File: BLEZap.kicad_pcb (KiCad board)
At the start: 2 copper layers, 38.1 x 22.9 mm, 12 parts, among them P1 PRG_HEADER, P2 INPUT_HEADER, P3 CONN_01X02, Q1 IRLML6344, U1 Core51822B

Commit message: PCB Ready
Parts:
- removed JP1, JP2: Jumper, Resistors_SMD:R_1206
- added REF**: MountingHole_2.7mm_M2.5, Mounting_Holes:MountingHole_2.7mm_M2.5, F.Cu at (89.7, 88.1)
- P1: footprint KevinLibrary:POGO_PIN_PAD_1X4 -> Pin_Headers:Pin_Header_Straight_1x04
- P2: footprint KevinLibrary:Pin_Header_Straight_1x04_HB -> Pin_Headers:Pin_Header_Straight_1x04
- moved P1 7.62 mm to (79.5, 78.7), turned to 90 degrees
- moved R4 7.03 mm to (87.4, 82.8)
- moved U1 2.30 mm to (103.9, 88.1), turned to 0 degrees
- moved P2 1.70 mm to (79.5, 96.8)
- moved Q1 1.61 mm to (85.1, 91.4)
- moved R2 1.52 mm to (78.7, 82.8)
- moved R1 1.31 mm to (81.5, 82.8)
- moved R3 1.13 mm to (84.3, 82.8)
- moved D1 1.05 mm to (81.5, 88.9)
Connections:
- P3 pad 1: Net-(JP2-Pad2) -> Net-(D1-Pad1)
- R2 pad 2: Net-(JP2-Pad2) -> Net-(D1-Pad1)
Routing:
- net Net-(JP2-Pad2): track 16.5 -> 0.00 mm
- net /RELAY: track 32.0 -> 16.9 mm, vias 0 -> 1
- net GNDD: track 24.5 -> 9.65 mm
- net /CFG_BTN: track 27.1 -> 17.9 mm, vias 0 -> 1
- net Net-(Q1-Pad1): track 0.00 -> 7.79 mm, vias 0 -> 2
- net Net-(R4-Pad2): track 13.6 -> 7.33 mm
- net /SWDIO: track 30.0 -> 26.7 mm, vias 0 -> 1
- net GND: track 13.2 -> 10.3 mm
- net /SWCLK: track 32.6 -> 29.9 mm, vias 0 -> 1
- net Net-(D1-Pad1): track 32.6 -> 30.3 mm
- net VDD: track 43.9 -> 42.5 mm
- added copper zone on B.Cu, net GNDD
- added copper zone on F.Cu, net GNDD
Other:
- net class Default: clearance 0.3048 -> 0.254; trace_width 0.3048 -> 0.1524; via_dia 2.54 -> 0.6858; via_drill 0.8382 -> 0.3302
- net class Power added: clearance 0.3048, trace_width 0.3048, via_dia 0.6858, via_drill 0.3302
- rule trace_clearance: 0.3048 -> 0.254
- rule trace_min: 0.3048 -> 0.1524
- rule via_min_drill: 0.8382 -> 0.3302
- rule via_min_size: 2.54 -> 0.6858

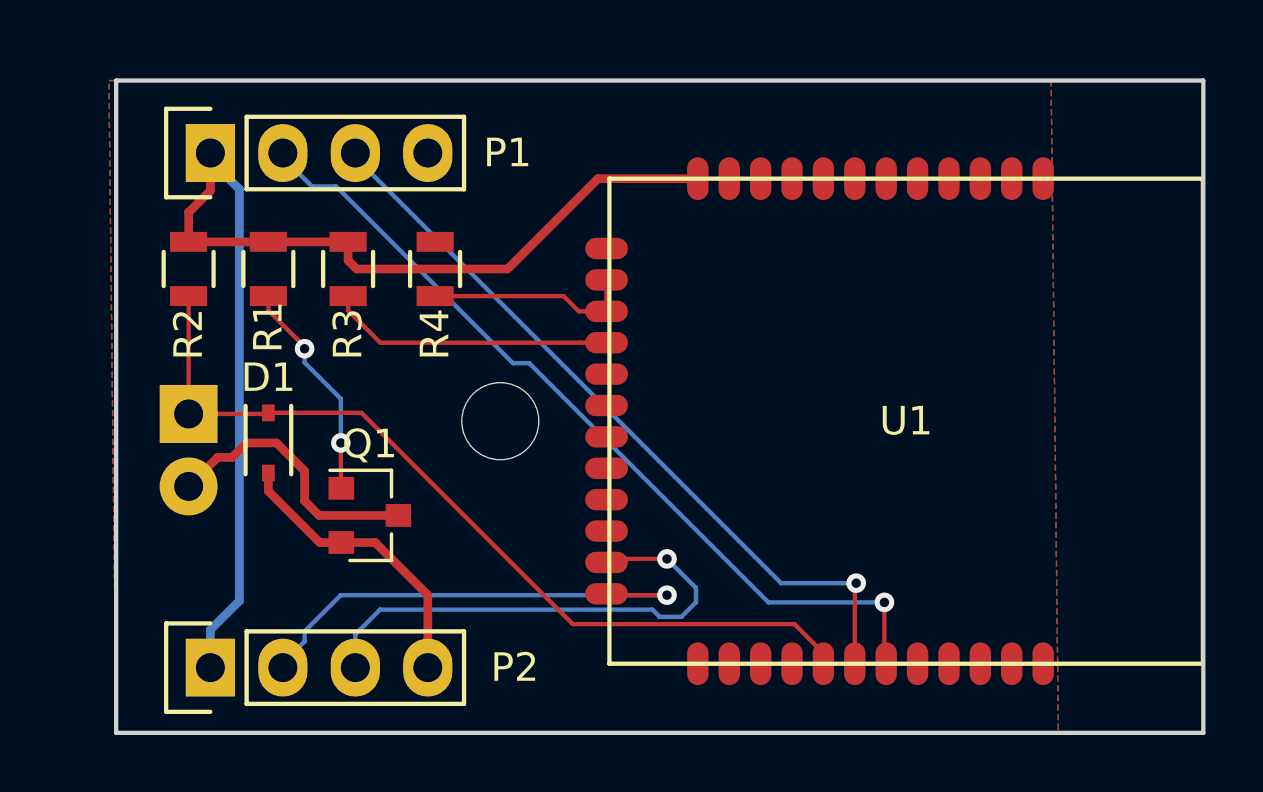
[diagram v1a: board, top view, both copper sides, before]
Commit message: SWD Swap
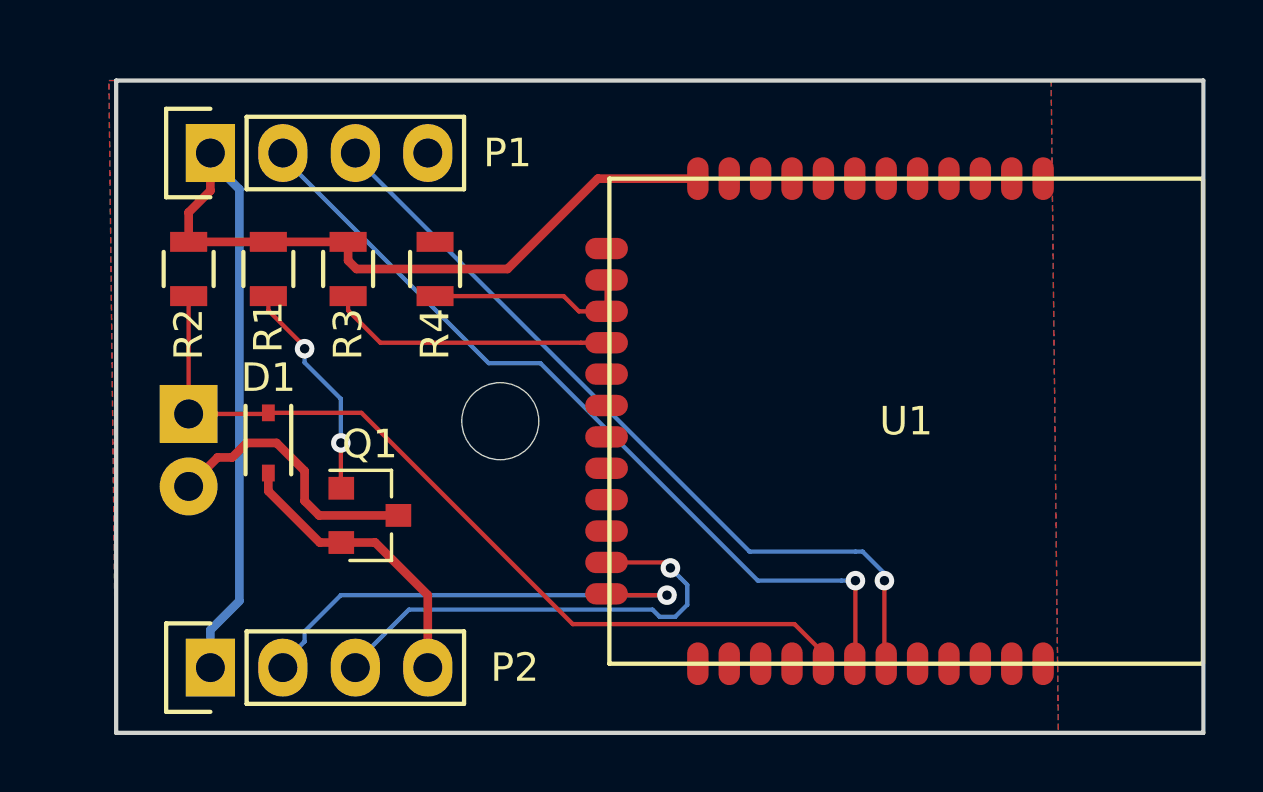
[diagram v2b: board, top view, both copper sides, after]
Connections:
- P1 pad 2: /SWCLK -> /SWDIO
- P1 pad 3: /SWDIO -> /SWCLK
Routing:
- net /SWDIO: track 26.7 -> 29.3 mm
- net /SWCLK: track 29.9 -> 27.9 mm
- net /CFG_BTN: track 17.9 -> 16.7 mm
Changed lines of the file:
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@@
     (links 23)
     (no_connects 0)
-    (area 67.760199 73.697104 114.665801 102.483562)
+    (area 76.124999 76.124999 114.375001 99.135001)
     (thickness 1.6)
     (drawings 4)
-    (tracks 94)
+    (tracks 96)
     (zones 0)
     (modules 11)
@@
   (layers
     (0 F.Cu signal)
-    (31 B.Cu signal hide)
-    (32 B.Adhes user hide)
-    (33 F.Adhes user hide)
-    (34 B.Paste user hide)
-    (35 F.Paste user hide)
-    (36 B.SilkS user hide)
+    (31 B.Cu signal)
+    (34 B.Paste user)
+    (35 F.Paste user)
+    (36 B.SilkS user)
     (37 F.SilkS user)
-    (38 B.Mask user hide)
-    (39 F.Mask user hide)
-    (44 Edge.Cuts user hide)
-    (48 B.Fab user hide)
-    (49 F.Fab user hide)
+    (38 B.Mask user)
+    (39 F.Mask user)
+    (44 Edge.Cuts user)
   )
   (setup
@@
       (net 5 VDD))
     (pad 2 thru_hole oval (at 0 2.54 90) (size 2.032 1.7272) (drill 1.016) (layers *.Cu *.Mask)
+      (net 7 /SWDIO))
+    (pad 3 thru_hole oval (at 0 5.08 90) (size 2.032 1.7272) (drill 1.016) (layers *.Cu *.Mask)
       (net 6 /SWCLK))
-    (pad 3 thru_hole oval (at 0 5.08 90) (size 2.032 1.7272) (drill 1.016) (layers *.Cu *.Mask)
-      (net 7 /SWDIO))
     (pad 4 thru_hole oval (at 0 7.62 90) (size 2.032 1.7272) (drill 1.016) (layers *.Cu *.Mask)
       (net 3 GNDD))
@@
   (segment (start 79.502 96.6216) (end 79.502 96.774) (width 0.3048) (layer F.Cu) (net 5))
   (segment (start 79.502 78.74) (end 79.502 78.8924) (width 0.3048) (layer B.Cu) (net 5))
-  (segment (start 82.042 78.74) (end 82.042 78.8924) (width 0.1524) (layer B.Cu) (net 6))
-  (segment (start 90.678 86.106) (end 99.06 94.488) (width 0.1524) (layer B.Cu) (net 6))
-  (segment (start 82.042 78.8924) (end 83.058 79.9084) (width 0.1524) (layer B.Cu) (net 6))
-  (segment (start 83.058 79.9084) (end 83.909698 79.9084) (width 0.1524) (layer B.Cu) (net 6))
-  (segment (start 83.909698 79.9084) (end 90.107298 86.106) (width 0.1524) (layer B.Cu) (net 6))
-  (segment (start 90.107298 86.106) (end 90.678 86.106) (width 0.1524) (layer B.Cu) (net 6))
-  (segment (start 99.06 94.488) (end 103.124 94.488) (width 0.1524) (layer B.Cu) (net 6))
-  (segment (start 103.124 94.488) (end 103.124 96.576) (width 0.1524) (layer F.Cu) (net 6))
+  (segment (start 103.124 93.726) (end 103.124 96.576) (width 0.1524) (layer F.Cu) (net 6))
   (segment (start 103.124 96.576) (end 103.186 96.638) (width 0.1524) (layer F.Cu) (net 6))
-  (via (at 103.124 94.488) (size 0.6858) (drill 0.3302) (layers F.Cu B.Cu) (net 6))
-  (segment (start 101.650053 93.81489) (end 102.134986 93.81489) (width 0.1524) (layer B.Cu) (net 7))
-  (segment (start 99.50449 93.81489) (end 101.650053 93.81489) (width 0.1524) (layer B.Cu) (net 7))
-  (segment (start 84.582 78.8924) (end 99.50449 93.81489) (width 0.1524) (layer B.Cu) (net 7))
-  (segment (start 102.086 93.863876) (end 102.134986 93.81489) (width 0.1524) (layer F.Cu) (net 7))
-  (segment (start 102.086 96.638) (end 102.086 93.863876) (width 0.1524) (layer F.Cu) (net 7))
-  (segment (start 84.582 78.74) (end 84.582 78.8924) (width 0.1524) (layer B.Cu) (net 7))
-  (via (at 102.134986 93.81489) (size 0.6858) (drill 0.3302) (layers F.Cu B.Cu) (net 7))
+  (segment (start 102.362 92.71) (end 103.124 93.472) (width 0.1524) (layer B.Cu) (net 6))
+  (segment (start 103.124 93.472) (end 103.124 93.726) (width 0.1524) (layer B.Cu) (net 6))
+  (via (at 103.124 93.726) (size 0.6858) (drill 0.3302) (layers F.Cu B.Cu) (net 6))
+  (segment (start 102.108 92.71) (end 102.362 92.71) (width 0.1524) (layer B.Cu) (net 6))
+  (segment (start 98.3996 92.71) (end 102.108 92.71) (width 0.1524) (layer B.Cu) (net 6))
+  (segment (start 84.582 78.74) (end 84.582 78.8924) (width 0.1524) (layer B.Cu) (net 6))
+  (segment (start 84.582 78.8924) (end 98.3996 92.71) (width 0.1524) (layer B.Cu) (net 6))
+  (segment (start 101.623067 93.726) (end 102.108 93.726) (width 0.1524) (layer B.Cu) (net 7))
+  (segment (start 91.068426 86.106) (end 98.688426 93.726) (width 0.1524) (layer B.Cu) (net 7))
+  (segment (start 89.2556 86.106) (end 91.068426 86.106) (width 0.1524) (layer B.Cu) (net 7))
+  (segment (start 82.042 78.8924) (end 89.2556 86.106) (width 0.1524) (layer B.Cu) (net 7))
+  (segment (start 82.042 78.74) (end 82.042 78.8924) (width 0.1524) (layer B.Cu) (net 7))
+  (segment (start 98.688426 93.726) (end 101.623067 93.726) (width 0.1524) (layer B.Cu) (net 7))
+  (segment (start 102.108 93.726) (end 102.108 96.616) (width 0.1524) (layer F.Cu) (net 7))
+  (segment (start 102.108 96.616) (end 102.086 96.638) (width 0.1524) (layer F.Cu) (net 7))
+  (via (at 102.108 93.726) (size 0.6858) (drill 0.3302) (layers F.Cu B.Cu) (net 7))
   (segment (start 95.504 94.234) (end 93.432 94.234) (width 0.1524) (layer F.Cu) (net 8))
   (segment (start 93.432 94.234) (end 93.386 94.188) (width 0.1524) (layer F.Cu) (net 8))
@@
   (segment (start 82.042 96.774) (end 82.042 96.6216) (width 0.1524) (layer B.Cu) (net 8))
   (segment (start 82.042 96.6216) (end 82.804 95.8596) (width 0.1524) (layer B.Cu) (net 8))
-  (segment (start 95.504 92.964) (end 93.51 92.964) (width 0.1524) (layer F.Cu) (net 9))
-  (segment (start 93.51 92.964) (end 93.386 93.088) (width 0.1524) (layer F.Cu) (net 9))
-  (segment (start 96.52 93.98) (end 95.504 92.964) (width 0.1524) (layer B.Cu) (net 9))
-  (via (at 95.504 92.964) (size 0.6858) (drill 0.3302) (layers F.Cu B.Cu) (net 9))
-  (segment (start 96.52 94.488) (end 96.52 93.98) (width 0.1524) (layer B.Cu) (net 9))
-  (segment (start 96.012 94.996) (end 96.52 94.488) (width 0.1524) (layer B.Cu) (net 9))
-  (segment (start 95.25 94.996) (end 96.012 94.996) (width 0.1524) (layer B.Cu) (net 9))
+  (segment (start 84.582 96.774) (end 84.582 96.6216) (width 0.1524) (layer B.Cu) (net 9))
+  (segment (start 84.582 96.6216) (end 86.4616 94.742) (width 0.1524) (layer B.Cu) (net 9))
+  (via (at 95.623674 93.281521) (size 0.6858) (drill 0.3302) (layers F.Cu B.Cu) (net 9))
+  (segment (start 96.215178 94.57068) (end 96.215178 93.873025) (width 0.1524) (layer B.Cu) (net 9))
   (segment (start 94.996 94.742) (end 95.25 94.996) (width 0.1524) (layer B.Cu) (net 9))
-  (segment (start 85.4456 94.742) (end 94.996 94.742) (width 0.1524) (layer B.Cu) (net 9))
-  (segment (start 84.582 96.774) (end 84.582 95.6056) (width 0.1524) (layer B.Cu) (net 9))
-  (segment (start 84.582 95.6056) (end 85.4456 94.742) (width 0.1524) (layer B.Cu) (net 9))
+  (segment (start 96.215178 93.873025) (end 95.966573 93.62442) (width 0.1524) (layer B.Cu) (net 9))
+  (segment (start 95.966573 93.62442) (end 95.623674 93.281521) (width 0.1524) (layer B.Cu) (net 9))
+  (segment (start 95.25 94.996) (end 95.789858 94.996) (width 0.1524) (layer B.Cu) (net 9))
+  (segment (start 86.4616 94.742) (end 94.996 94.742) (width 0.1524) (layer B.Cu) (net 9))
+  (segment (start 95.430153 93.088) (end 95.623674 93.281521) (width 0.1524) (layer F.Cu) (net 9))
+  (segment (start 93.386 93.088) (end 95.430153 93.088) (width 0.1524) (layer F.Cu) (net 9))
+  (segment (start 95.789858 94.996) (end 96.215178 94.57068) (width 0.1524) (layer B.Cu) (net 9))
   (segment (start 84.328 83.754) (end 84.328 84.2564) (width 0.1524) (layer F.Cu) (net 10))
   (segment (start 92.4836 85.388) (end 93.386 85.388) (width 0.1524) (layer F.Cu) (net 10))
